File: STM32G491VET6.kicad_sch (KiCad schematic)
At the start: 21 parts, among them U3 STM32G431CBT6, X1 X50328MSB2GI, Y1 SSPT7F-7PF20-R

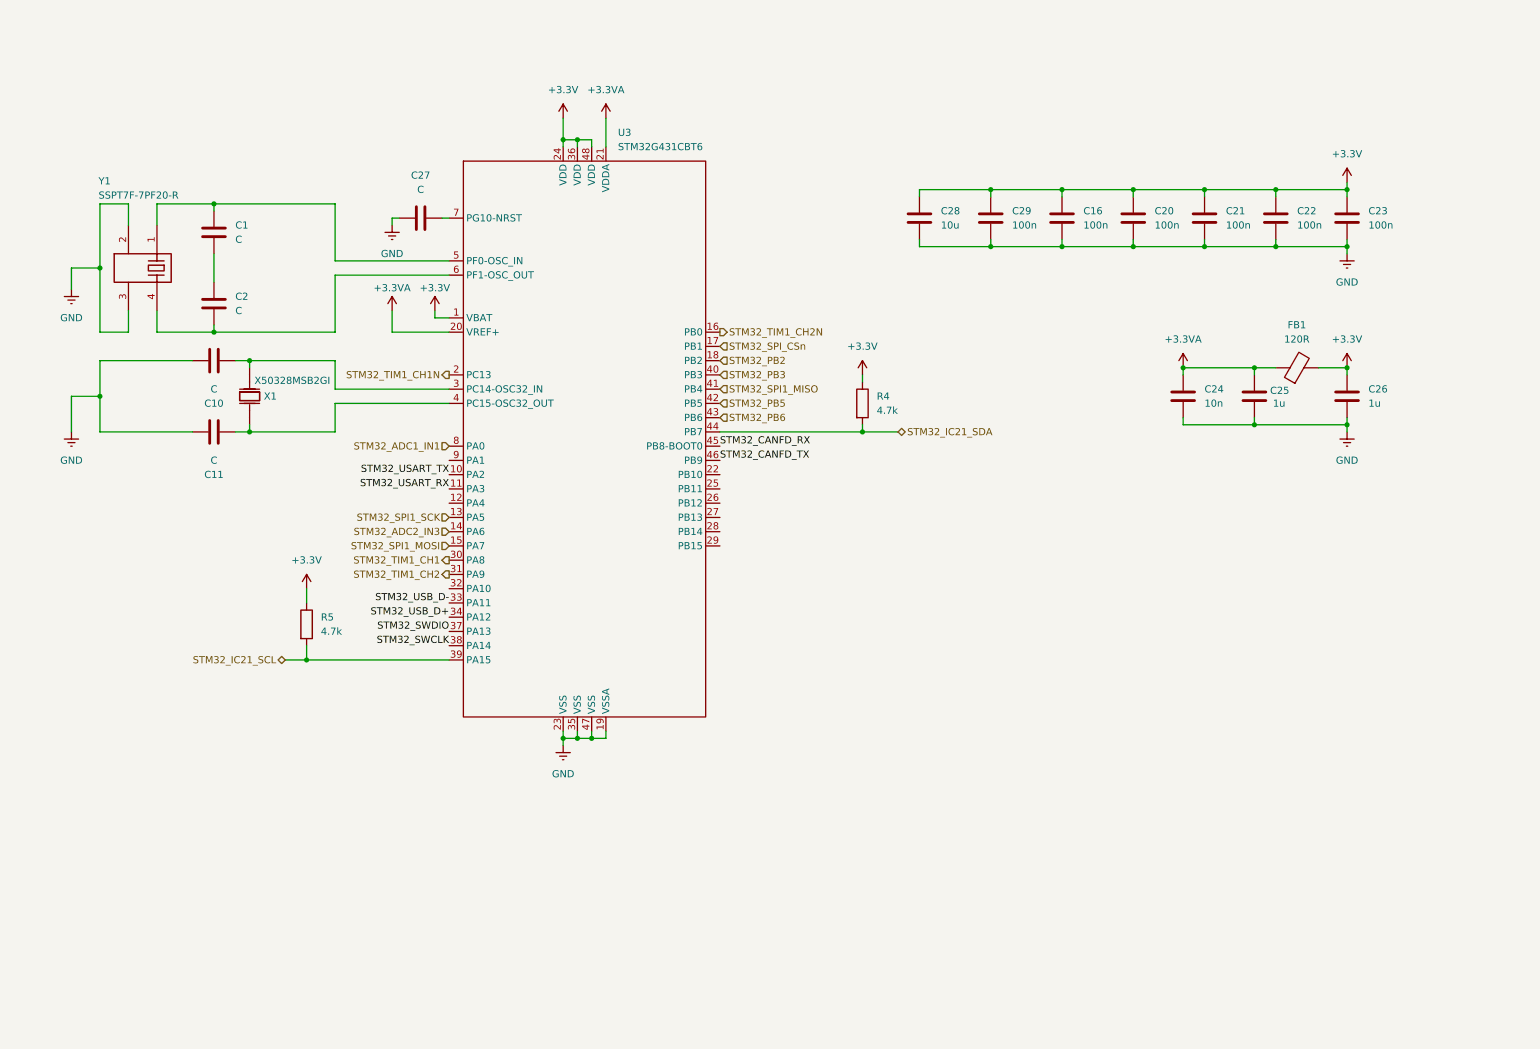
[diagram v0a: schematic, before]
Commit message: feat: add can and usart connector
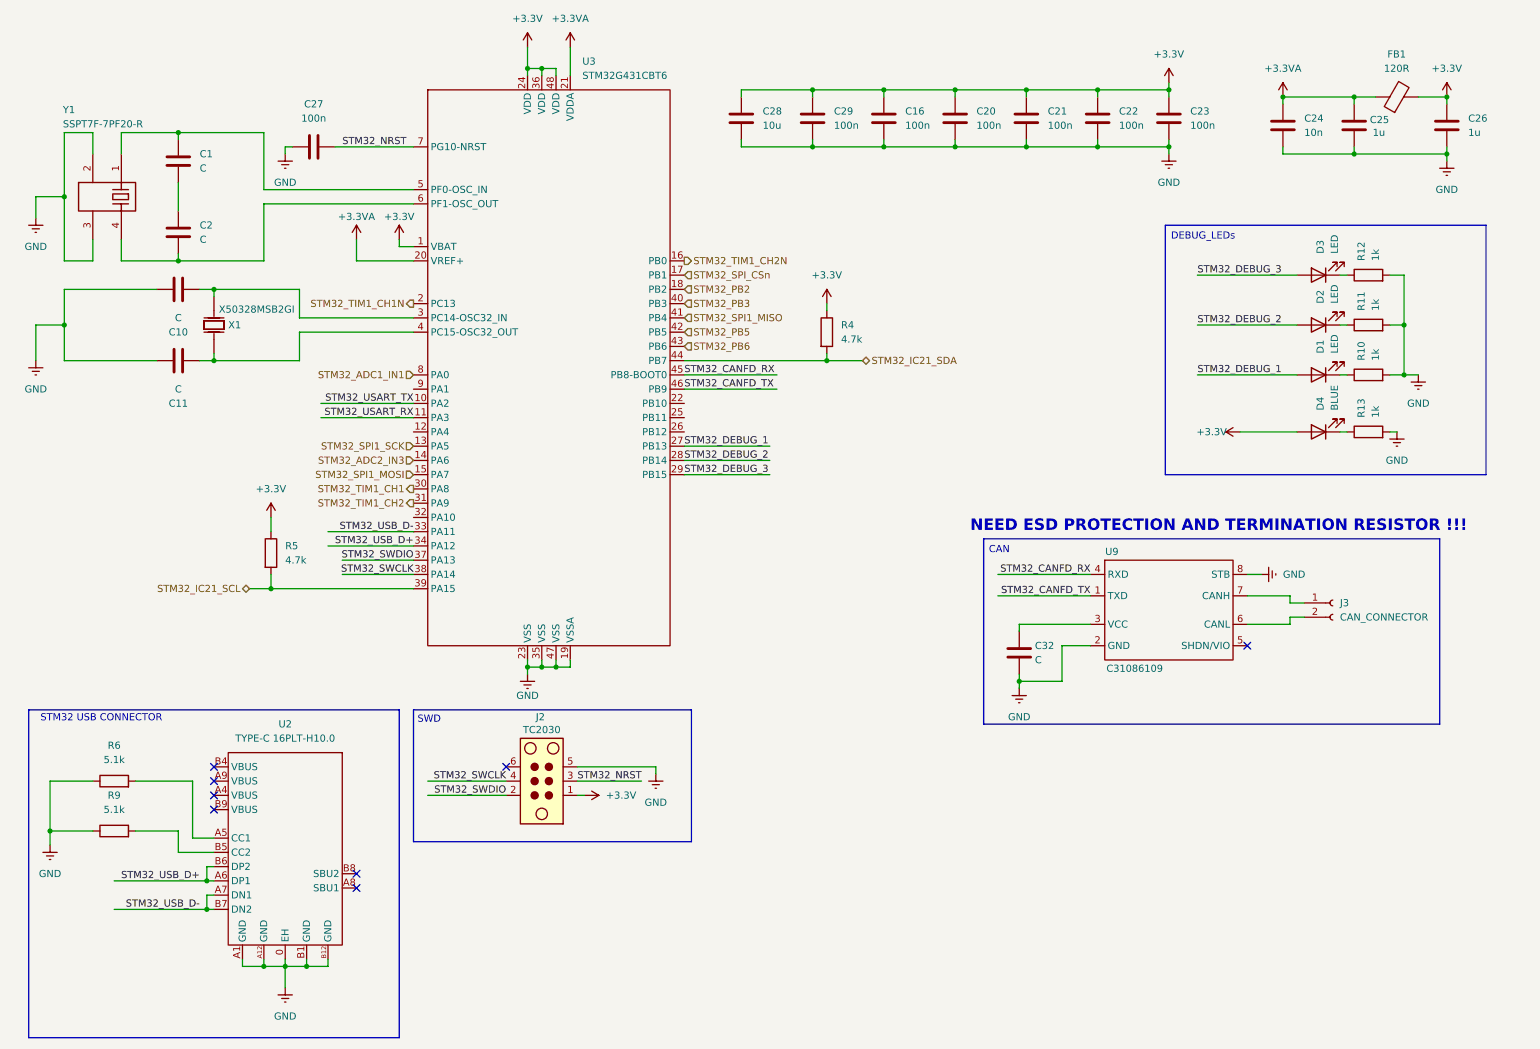
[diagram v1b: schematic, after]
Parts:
- added C32: C, symbol Device:C
- added D1, D2, D3: LED, symbol Device:LED
- added D4: BLUE, symbol Device:LED
- added J2: TC2030, Connector:Tag-Connect_TC2030-IDC-NL_2x03_P1.27mm_Vertical, symbol Connector:TC2030
- added J3: CAN_CONNECTOR, symbol Connector:Conn_01x02_Socket
- added R10, R11, R12, R13: 1k, symbol Device:R
- added R6, R9: 5.1k, symbol Device:R
- added U2: TYPE-C 16PLT-H10.0, EasyEDA_Lib:TYPE-C-SMD_USB4120-03-C, symbol EasyEDA_Lib:TYPE-C 16PLT-H10.0
- added U9: C31086109, EasyEDA_Lib:SOP-8_L4.9-W3.9-P1.27-LS6.0-BL, symbol EasyEDA_Lib:TCAN3403DRQ1
- C27: value C -> 100n
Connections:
- net +3.3V: now also D4.2 (A), J2.1
- net GND: now also C32.2, J2.5, R10.2, R11.2, R12.2, R13.2, R6.1, R9.1, U2.0 (EH), U2.A1 (GND), U2.A12 (GND), U2.B1 (GND), U2.B12 (GND), U9.2 (GND), U9.8 (STB)
- net STM32_CANFD_RX: now also U9.4 (RXD)
- net STM32_CANFD_TX: now also U9.1 (TXD)
- net STM32_SWCLK: now also J2.4
- net STM32_SWDIO: now also J2.2
- net STM32_USB_D+: now also U2.A6 (DP1), U2.B6 (DP2)
- net STM32_USB_D-: now also U2.A7 (DN1), U2.B7 (DN2)
- net STM32_DEBUG_1: now reaches U3.27 (PB13)
- net STM32_DEBUG_1: now also D1.2 (A)
- net STM32_DEBUG_2: now reaches U3.28 (PB14)
- net STM32_DEBUG_2: now also D2.2 (A)
- net STM32_DEBUG_3: now reaches U3.29 (PB15)
- net STM32_DEBUG_3: now also D3.2 (A)
- net STM32_NRST: now reaches C27.2, U3.7 (PG10-NRST)
- net STM32_NRST: now also J2.3
- new net: R9.2, U2.B5 (CC2)
- new net: D1.1 (K), R10.1
- new net: J3.1 (Pin_1), U9.7 (CANH)
- new net: J3.2 (Pin_2), U9.6 (CANL)
- new net: R6.2, U2.A5 (CC1)
- new net: D2.1 (K), R11.1
- new net: C32.1, U9.3 (VCC)
- new net: D4.1 (K), R13.1
- new net: D3.1 (K), R12.1
- no-connect marks 0 -> 8
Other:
- note added: "CAN"
- note added: "DEBUG_LEDs"
- note added: "NEED ESD PROTECTION AND TERMINATION RESISTOR !!!"
- note added: "STM32 USB CONNECTOR"
- note added: "SWD"
- moved on the sheet: C1, C10, C11, C16, C2, C20, C21, C22, C23, C24, C25, C26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

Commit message: change components
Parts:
- removed C20, C21: 100n, symbol Device:C
- removed D4: BLUE, symbol Device:LED
- removed R13: 1k, symbol Device:R
- removed X1: X50328MSB2GI, EasyEDA_Lib:CRYSTAL-SMD_L5.0-W3.2, symbol EasyEDA_Lib:X50328MSB2GI
- removed Y1: SSPT7F-7PF20-R, EasyEDA_Lib:MC-146_4P-L6.7-W1.5-P0.85-BL, symbol EasyEDA_Lib:32.768kHz
- added C33: 47u, Capacitor_SMD:C_0402_1005Metric, symbol Device:C
- added D5: ESD2CANFD24DBZR, EasyEDA_Lib:SOT-23-3_L2.9-W1.3-P1.90-LS2.4-BL-2, symbol EasyEDA_Lib:ESD2CANFD24DBZR
- added D8: USBLC6-2SC6, EasyEDA_Lib:SOT-23-6_L2.9-W1.6-P0.95-LS2.8-BL, symbol EasyEDA_Lib:USBLC6-2SC6
- added J4: USART CONNECTOR, symbol Connector:Conn_01x03_Socket
- added R14, R15: 60, PCM_Resistor_SMD_AKL:R_0402_1005Metric, symbol Device:R
- added X1: NX3215SA 32.768KHZ EXS00A-MU00525, EasyEDA_Lib:CRYSTAL-SMD_L3.2-W1.5, symbol EasyEDA_Lib:NX3215SA 32.768KHZ EXS00A-MU00525
- added X2: NDK NX2016SA-24MHZ-EXS00A-CS10820, PCM_Crystal_AKL:Crystal_SMD_2016-4Pin_2.0x1.6mm, symbol PCM_Crystal_AKL:SMD2016-4
- C1, C2: value C -> 6.8p; footprint (none) -> Capacitor_SMD:C_0402_1005Metric
- C10, C11: value C -> 5.1p; footprint (none) -> PCM_JLCPCB:C_0603
- C16, C22, C23, C24, C25, C26, C27, C29: footprint (none) -> Capacitor_SMD:C_0402_1005Metric
- C28: value 10u -> 4.7u; footprint (none) -> Capacitor_SMD:C_0402_1005Metric
- C32: value C -> 10n; footprint (none) -> Capacitor_SMD:C_0402_1005Metric
- R10, R11, R12, R4, R5, R6, R9: footprint (none) -> PCM_Resistor_SMD_AKL:R_0402_1005Metric
- U9: value C31086109 -> TCAN3403DRQ1
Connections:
- net GND: now also C1.2, C2.2, C33.2, D5.3 (GND), D8.2, J4.3 (Pin_3), X2.2, X2.4
- net STM32_DEBUG_1: now also D2.2 (A); no longer D1.2 (A)
- net STM32_DEBUG_2: now also D1.2 (A); no longer D2.2 (A)
- net STM32_SWCLK: no longer U3.38 (PA14)
- net STM32_SWDIO: no longer U3.37 (PA13)
- net STM32_USART_RX: now also J4.2 (Pin_2)
- net STM32_USART_TX: now also J4.1 (Pin_1)
- net STM32_USB_D+: now also D8.3; no longer U2.A6 (DP1), U2.B6 (DP2)
- net STM32_USB_D-: now also D8.1; no longer U2.A7 (DN1), U2.B7 (DN2)
- net OSC32_IN: now reaches C1.1
- net OSC32_IN: now also U3.3 (PC14-OSC32_IN), X2.1; no longer U3.5 (PF0-OSC_IN)
- net OSC32_OUT: now reaches C2.1
- net OSC32_OUT: now also U3.4 (PC15-OSC32_OUT), X2.3; no longer C1.2
- net OSC_OUT: now reaches C11.1
- net OSC_OUT: now also U3.6 (PF1-OSC_OUT), X1.1; no longer U3.4 (PC15-OSC32_OUT)
- net at J3.1 (Pin_1), U9.7 (CANH): now also D5.2 (IO), R14.1
- net at J3.2 (Pin_2), U9.6 (CANL): now also D5.1 (IO), R15.2
- net at U2.A4 (VBUS): now also U2.A9 (VBUS), U2.B4 (VBUS), U2.B9 (VBUS), D8.5
- net OSC_IN: now reaches C10.1
- net OSC_IN: now also U3.5 (PF0-OSC_IN), X1.2; no longer U3.3 (PC14-OSC32_IN)
- net +24V: now reaches U9.5 (SHDN/VIO)
- new net: C33.1, R14.2, R15.1
- new net: D8.4, U2.A6 (DP1), U2.B6 (DP2)
- new net: D8.6, U2.A7 (DN1), U2.B7 (DN2)
- no-connect marks 8 -> 7
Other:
- note added: "24Mhz Clock"
- note added: "32khz Clock"
- note added: "CAN CONNECTOR"
- note added: "CC0402CRNPO9BN5R1"
- note added: "CC0402CRNPO9BN6R8"
- note added: "MCU POWER SOURCE"
- note added: "SWD CONNECTOR (TAG Connector)"
- note added: "TVS Protection"
- note added: "USART1 CONNECTOR"
- note added: "USB CONNECTOR"
- note removed: "CAN"
- note removed: "NEED ESD PROTECTION AND TERMINATION RESISTOR !!!"
- note removed: "STM32 USB CONNECTOR"
- note removed: "SWD"
- moved on the sheet: C16, C22, C23, C24, C25, C26, C27, C28, C29, C32, D3, FB1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

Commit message: update sch
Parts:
- D1, D2, D3: footprint (none) -> LED_SMD:LED_0603_1608Metric
- FB1: footprint (none) -> PCM_Ferrite_SMD_AKL:Ferrite_0201_0603Metric
- J3: footprint (none) -> TerminalBlock:TerminalBlock_Xinya_XY308-2.54-2P_1x02_P2.54mm_Horizontal
- J4: footprint (none) -> TerminalBlock:TerminalBlock_Xinya_XY308-2.54-3P_1x03_P2.54mm_Horizontal
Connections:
- net STM32_SWCLK: now also U3.38 (PA14)
- net STM32_SWDIO: now also U3.37 (PA13)
- net STM32_USB_D+: now also D8.1; no longer D8.3
- net STM32_USB_D-: now also D8.3; no longer D8.1
- net at U2.A6 (DP1), U2.B6 (DP2): now also D8.6; no longer D8.4
- net at U2.A7 (DN1), U2.B7 (DN2): now also D8.4; no longer D8.6
- no-connect marks 7 -> 9
